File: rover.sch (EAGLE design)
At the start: 16 parts, among them IC1 MC33269ST-5.0T3, J1 B02B-PASK(LF)(SN)

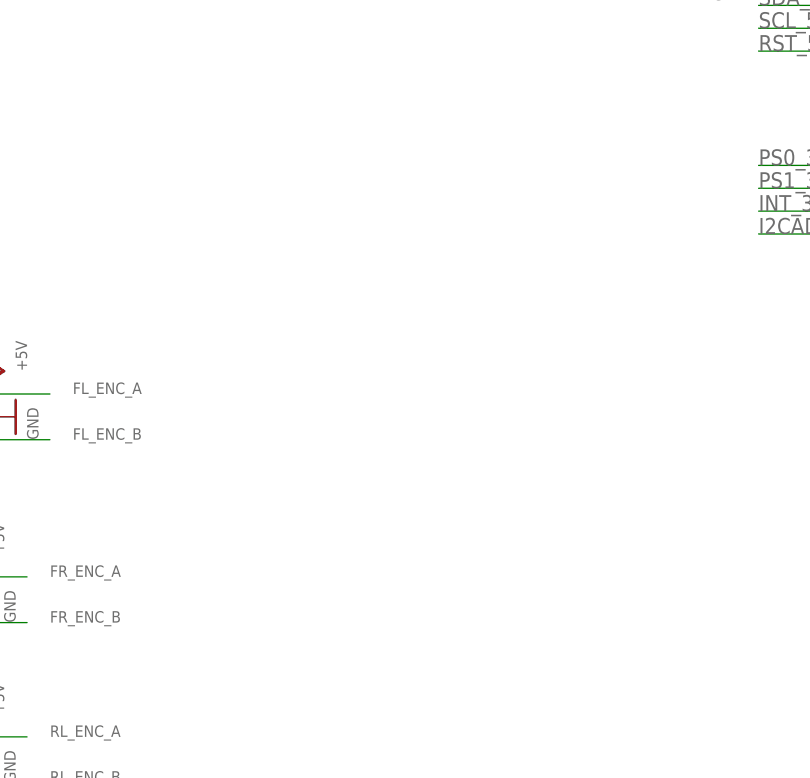
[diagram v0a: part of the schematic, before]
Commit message: added esc and servo headers
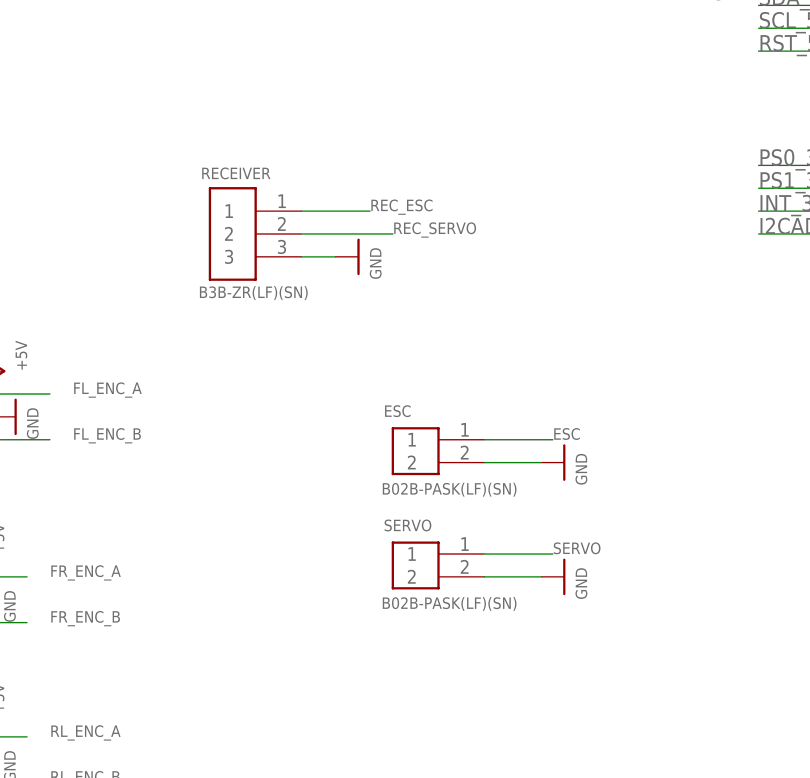
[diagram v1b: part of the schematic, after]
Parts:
- added ESC, SERVO: B02B-PASK(LF)(SN), Headers:B02B-PASK(LF)(SN)
- added RECEIVER: B3B-ZR(LF)(SN), Headers:B3B-ZR(LF)(SN)
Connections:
- net ESC: now also ESC.1
- net GND: now also ESC.2, RECEIVER.3, SERVO.2
- net REC_ESC: now also RECEIVER.1
- net REC_SERVO: now also RECEIVER.2
- net SERVO: now also SERVO.1
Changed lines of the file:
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@@
 <part name="P+4" library="supply1" library_urn="urn:adsk.eagle:library:371" deviceset="+5V" device=""/>
 <part name="GND2" library="SparkFun" deviceset="GND" device=""/>
+<part name="RECEIVER" library="Headers" library_urn="urn:adsk.eagle:library:11687645" deviceset="B3B-ZR(LF)(SN)" device="" package3d_urn="urn:adsk.eagle:package:19181366/2"/>
+<part name="GND3" library="SparkFun" deviceset="GND" device=""/>
+<part name="ESC" library="Headers" library_urn="urn:adsk.eagle:library:11687645" deviceset="B02B-PASK(LF)(SN)" device="" package3d_urn="urn:adsk.eagle:package:19181365/13"/>
+<part name="GND14" library="SparkFun" deviceset="GND" device=""/>
+<part name="SERVO" library="Headers" library_urn="urn:adsk.eagle:library:11687645" deviceset="B02B-PASK(LF)(SN)" device="" package3d_urn="urn:adsk.eagle:package:19181365/13"/>
+<part name="GND15" library="SparkFun" deviceset="GND" device=""/>
 </parts>
 <sheets>
@@
 <attribute name="VALUE" x="80.01" y="116.84" size="1.27" layer="96" rot="R90"/>
 </instance>
+<instance part="RECEIVER" gate="G$1" x="27.94" y="76.2" smashed="yes">
+<attribute name="NAME" x="24.384" y="82.296" size="1.27" layer="95"/>
+<attribute name="VALUE" x="24.13" y="69.088" size="1.27" layer="96"/>
+</instance>
+<instance part="GND3" gate="1" x="41.91" y="73.66" smashed="yes" rot="R90">
+<attribute name="VALUE" x="44.45" y="71.12" size="1.27" layer="96" rot="R90"/>
+</instance>
+<instance part="ESC" gate="G$1" x="48.26" y="50.8" smashed="yes">
+<attribute name="NAME" x="44.704" y="55.88" size="1.27" layer="95"/>
+<attribute name="VALUE" x="44.45" y="47.244" size="1.27" layer="96"/>
+</instance>
+<instance part="GND14" gate="1" x="64.77" y="50.8" smashed="yes" rot="R90">
+<attribute name="VALUE" x="67.31" y="48.26" size="1.27" layer="96" rot="R90"/>
+</instance>
+<instance part="SERVO" gate="G$1" x="48.26" y="38.1" smashed="yes">
+<attribute name="NAME" x="44.704" y="43.18" size="1.27" layer="95"/>
+<attribute name="VALUE" x="44.45" y="34.544" size="1.27" layer="96"/>
+</instance>
+<instance part="GND15" gate="1" x="64.77" y="38.1" smashed="yes" rot="R90">
+<attribute name="VALUE" x="67.31" y="35.56" size="1.27" layer="96" rot="R90"/>
+</instance>
 </instances>
 <busses>
@@
 <wire x1="71.12" y1="119.38" x2="74.93" y2="119.38" width="0.1524" layer="91"/>
 </segment>
+<segment>
+<pinref part="RECEIVER" gate="G$1" pin="3"/>
+<pinref part="GND3" gate="1" pin="GND"/>
+<wire x1="35.56" y1="73.66" x2="39.37" y2="73.66" width="0.1524" layer="91"/>
+</segment>
+<segment>
+<pinref part="ESC" gate="G$1" pin="2"/>
+<pinref part="GND14" gate="1" pin="GND"/>
+<wire x1="55.88" y1="50.8" x2="62.23" y2="50.8" width="0.1524" layer="91"/>
+</segment>
+<segment>
+<pinref part="SERVO" gate="G$1" pin="2"/>
+<pinref part="GND15" gate="1" pin="GND"/>
+<wire x1="55.88" y1="38.1" x2="62.23" y2="38.1" width="0.1524" layer="91"/>
+</segment>
 </net>
 <net name="SDA_5V" class="0">
@@
 <pinref part="U$5" gate="G$1" pin="2"/>
 </segment>
+<segment>
+<pinref part="SERVO" gate="G$1" pin="1"/>
+<wire x1="55.88" y1="40.64" x2="63.5" y2="40.64" width="0.1524" layer="91"/>
+<label x="63.5" y="40.64" size="1.27" layer="95"/>
+</segment>
 </net>
 <net name="ESC" class="0">
@@
 <pinref part="U$5" gate="G$1" pin="3"/>
 </segment>
+<segment>
+<pinref part="ESC" gate="G$1" pin="1"/>
+<wire x1="55.88" y1="53.34" x2="63.5" y2="53.34" width="0.1524" layer="91"/>
+<label x="63.5" y="53.34" size="1.27" layer="95"/>
+</segment>
 </net>
 <net name="RR_ENC_B" class="0">
@@
 <pinref part="U$5" gate="G$1" pin="14/A0/TX3"/>
 </segment>
+<segment>
+<pinref part="RECEIVER" gate="G$1" pin="2"/>
+<wire x1="35.56" y1="76.2" x2="45.72" y2="76.2" width="0.1524" layer="91"/>
+<label x="45.72" y="76.2" size="1.27" layer="95"/>
+</segment>
 </net>
 <net name="REC_ESC" class="0">
@@
 <pinref part="U$5" gate="G$1" pin="15/A1/RX3"/>
 </segment>
-</net>
+<segment>
+<pinref part="RECEIVER" gate="G$1" pin="1"/>
+<wire x1="35.56" y1="78.74" x2="43.18" y2="78.74" width="0.1524" layer="91"/>
+<label x="43.18" y="78.74" size="1.27" layer="95"/>
+</segment>
+</net>

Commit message: added ground planes
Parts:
- C1, C2, D1, ESC, FL_ENC, FR_ENC, GREEN, IC1, J1, JP3, JP4, R1, RECEIVER, RL_ENC, RR_ENC, S1, SERVO, STEER_ENC, U$5: OC_NEWARK (none) -> unknown

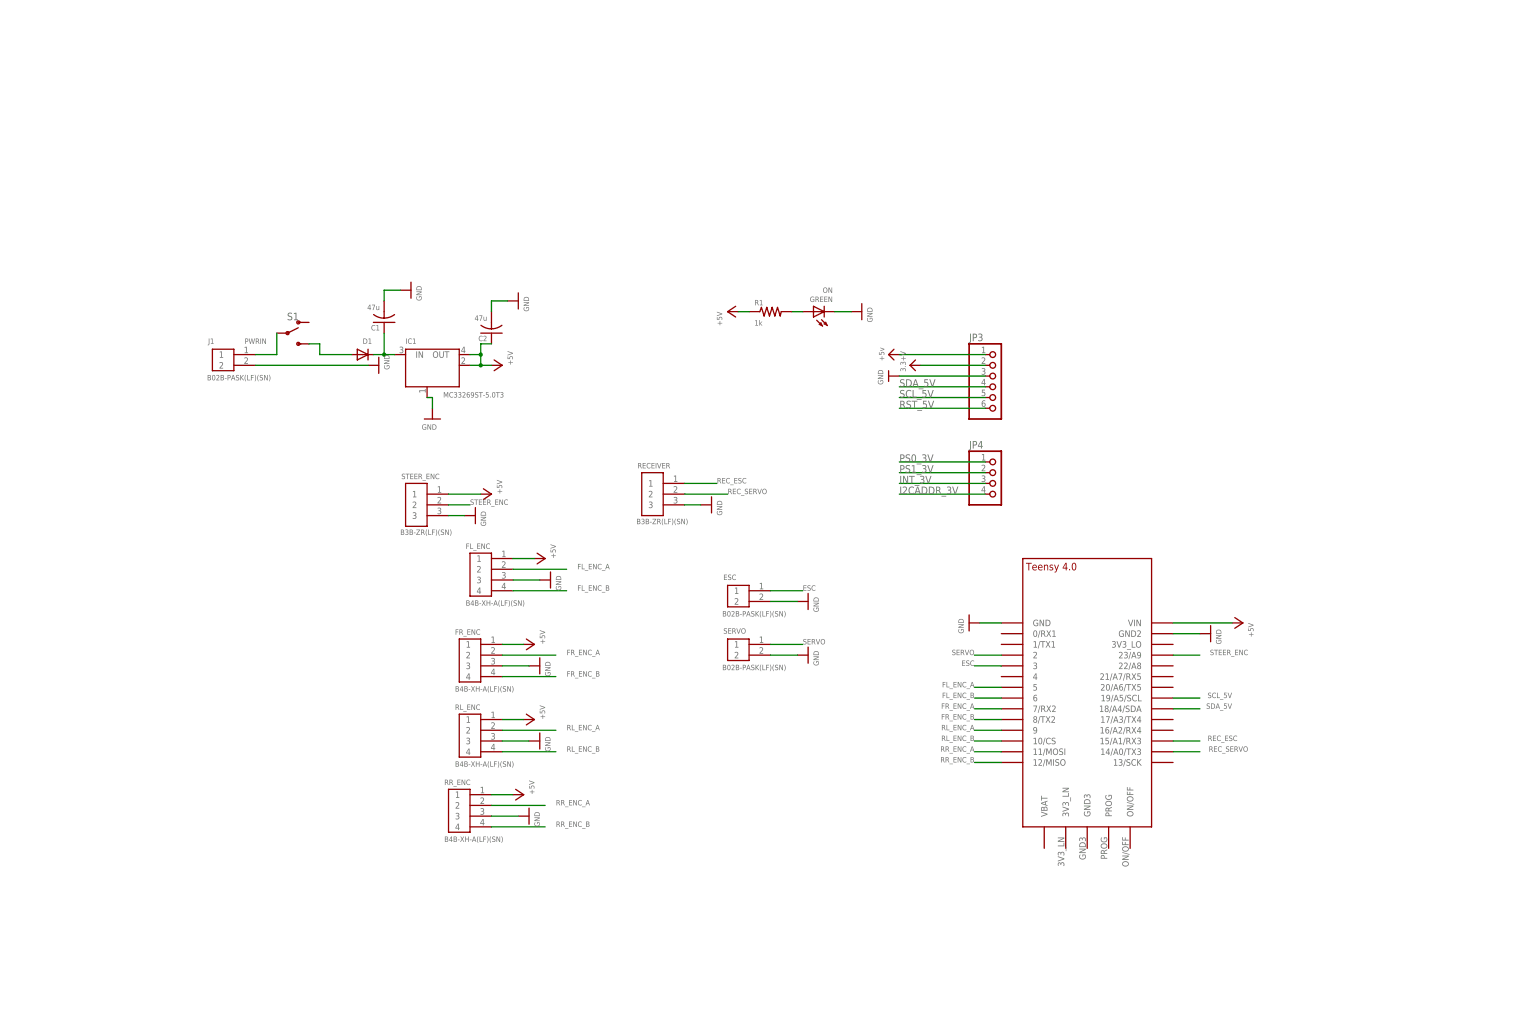
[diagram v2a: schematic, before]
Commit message: organized schematic
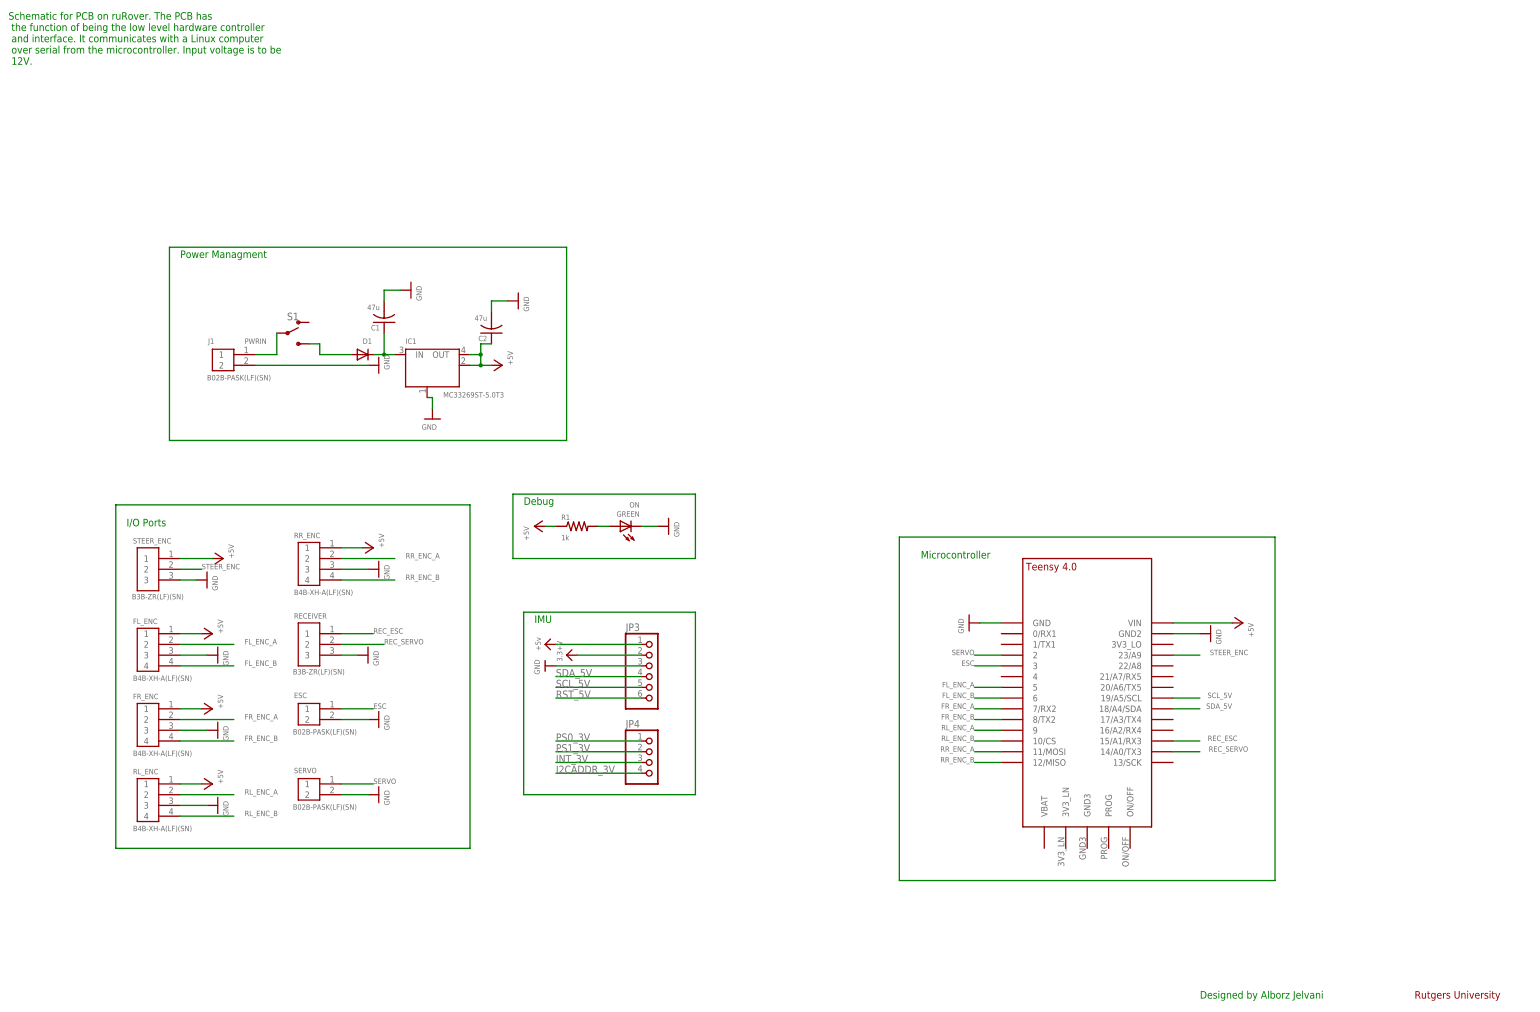
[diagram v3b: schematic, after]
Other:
- note added: "Debug"
- note added: "Designed by Alborz Jelvani"
- note added: "I/O Ports"
- note added: "IMU"
- note added: "Microcontroller"
- note added: "Power Managment"
- note added: "Rutgers University"
- note added: "Schematic for PCB on ruRover. The PCB has the function of being the low level hardware controller and interface. It communicates with a Linux computer over serial from the microcontroller. Input voltage is to be 12V."
- moved on the sheet: ESC, FL_ENC, FR_ENC, GREEN, JP3, JP4, R1, RECEIVER, RL_ENC, RR_ENC, SERVO, STEER_ENC
